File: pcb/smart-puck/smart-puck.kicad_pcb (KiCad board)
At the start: 2 copper layers, 77.4 x 79 mm, 13 parts, among them SW1 ILS TA180 40, SW3 ILS TA180 40, U1 Pico

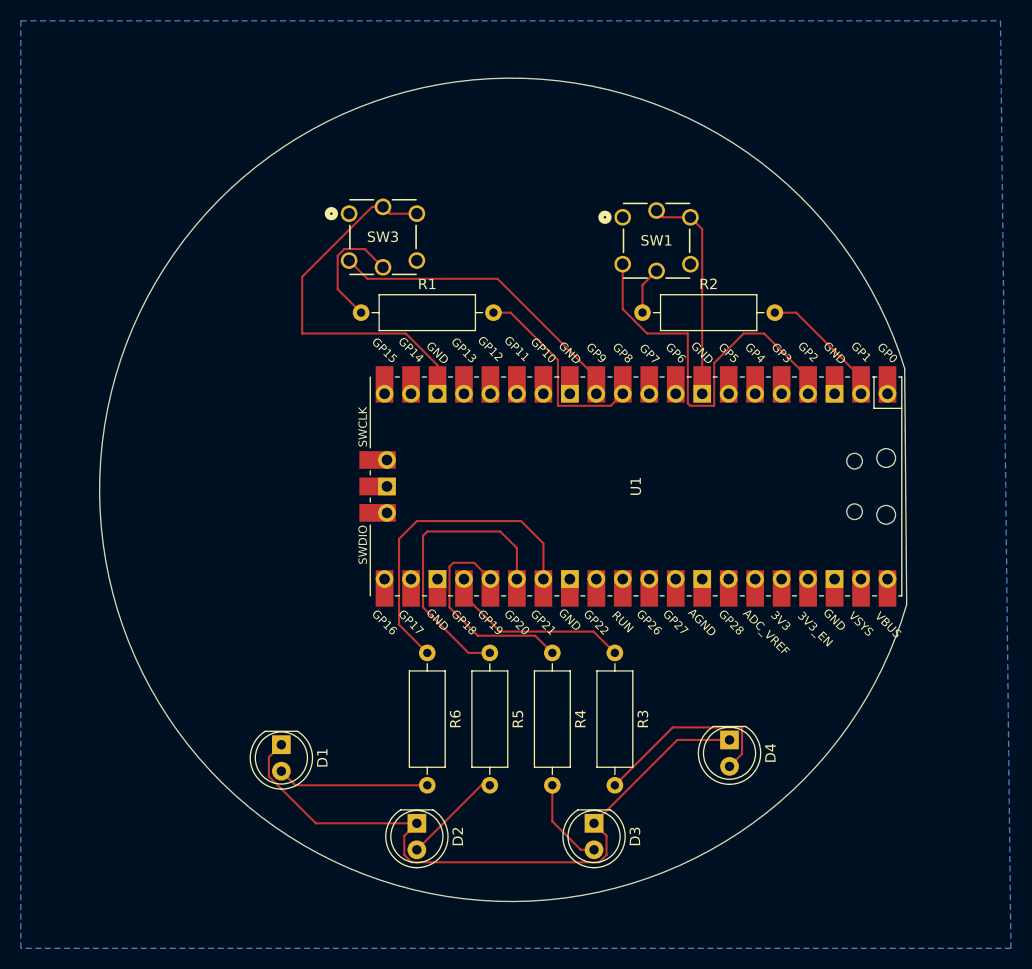
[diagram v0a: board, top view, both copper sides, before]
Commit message: update PCB. Align components. Add some mounting holes. Add a big hole in case we need to mount the doorbell stuff underneath
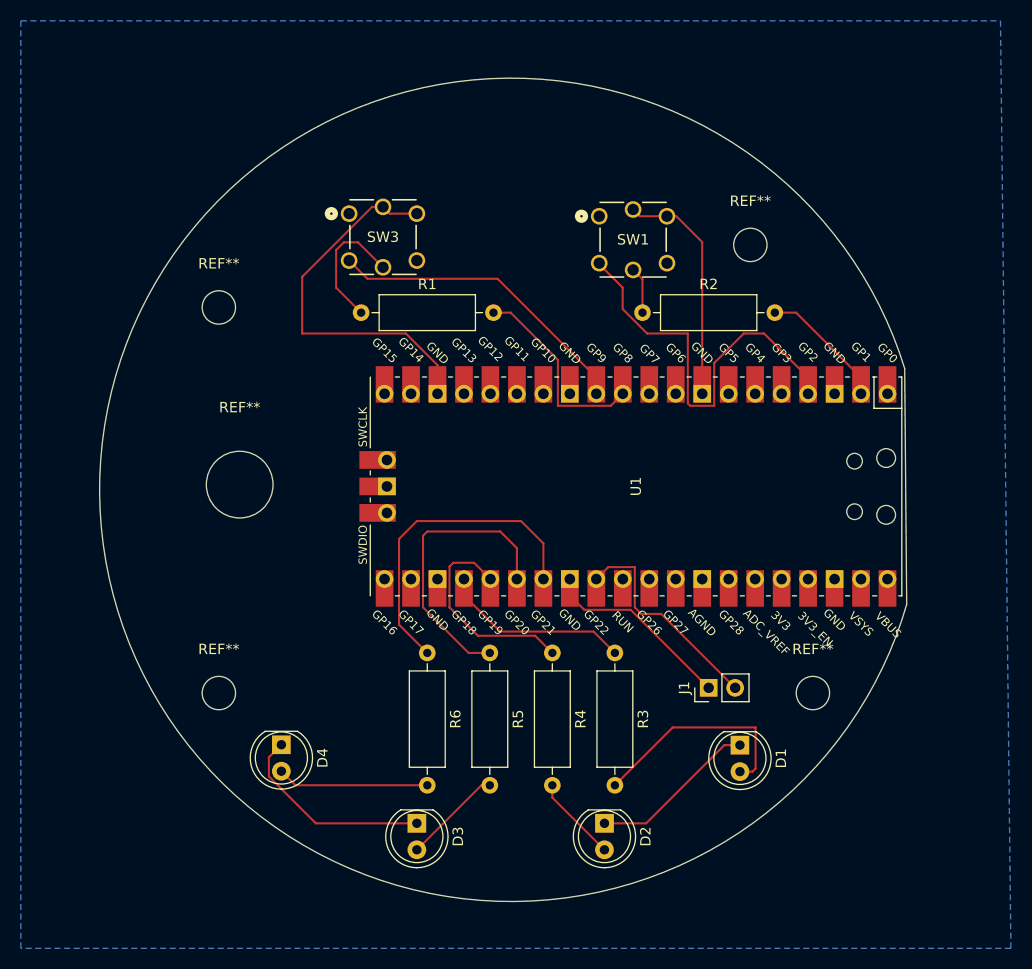
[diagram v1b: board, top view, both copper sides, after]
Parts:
- added J1: Conn_01x02_Pin, Connector_PinHeader_2.54mm:PinHeader_1x02_P2.54mm_Vertical, F.Cu at (163.0, 116.0)
- added REF**: MountingHole_3.2mm_M3, MountingHole:MountingHole_3.2mm_M3, F.Cu at (116.0, 79.5)
- added REF**: MountingHole_3.2mm_M3, MountingHole:MountingHole_3.2mm_M3, F.Cu at (167.0, 73.5)
- added REF**: MountingHole_6.4mm_M6, MountingHole:MountingHole_6.4mm_M6, F.Cu at (118.0, 96.5)
- added REF**: MountingHole_3.2mm_M3, MountingHole:MountingHole_3.2mm_M3, F.Cu at (116.0, 116.5)
- added REF**: MountingHole_3.2mm_M3, MountingHole:MountingHole_3.2mm_M3, F.Cu at (173.0, 116.5)
- moved SW1 2.25 mm to (152.5, 70.8)
- moved D1 1.12 mm to (166.0, 121.5)
- moved D2 1.00 mm to (153.0, 129.0)
- renumbered D4 to D1, D3 to D2, D2 to D3, D1 to D4
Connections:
- net GND renamed Net-(D1-K)
- U1 pad 28: unconnected-(U1-GND-Pad28) -> Net-(J1-Pin_1)
- U1 pad 29: unconnected-(U1-GPIO22-Pad29)_1 -> Net-(J1-Pin_2)
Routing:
- net Net-(D1-K): track 63.0 -> 35.7 mm
- net Net-(J1-Pin_2): track 0.00 -> 20.9 mm
- net Net-(J1-Pin_1): track 0.00 -> 18.6 mm
- net Net-(D1-A): track 18.7 -> 21.4 mm
- net Net-(SW1-Pad2): track 20.9 -> 22.5 mm
- net Net-(R1-Pad1): track 11.7 -> 12.8 mm
- net Net-(U1-GPIO2): track 38.5 -> 39.5 mm
